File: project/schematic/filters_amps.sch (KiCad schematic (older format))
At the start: 19 parts

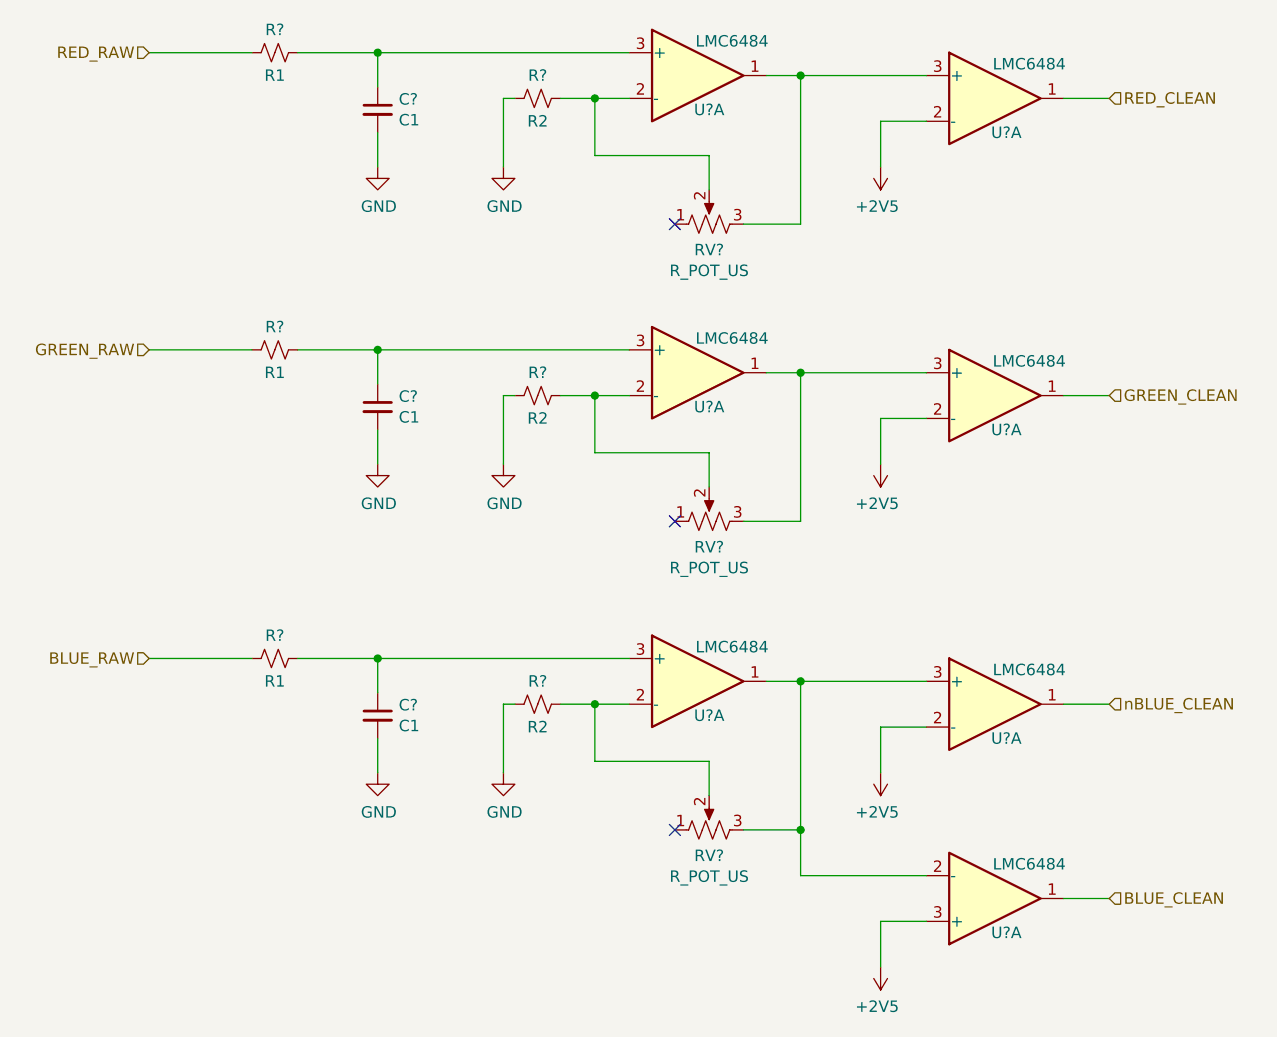
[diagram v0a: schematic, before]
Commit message: switch to high pass filters
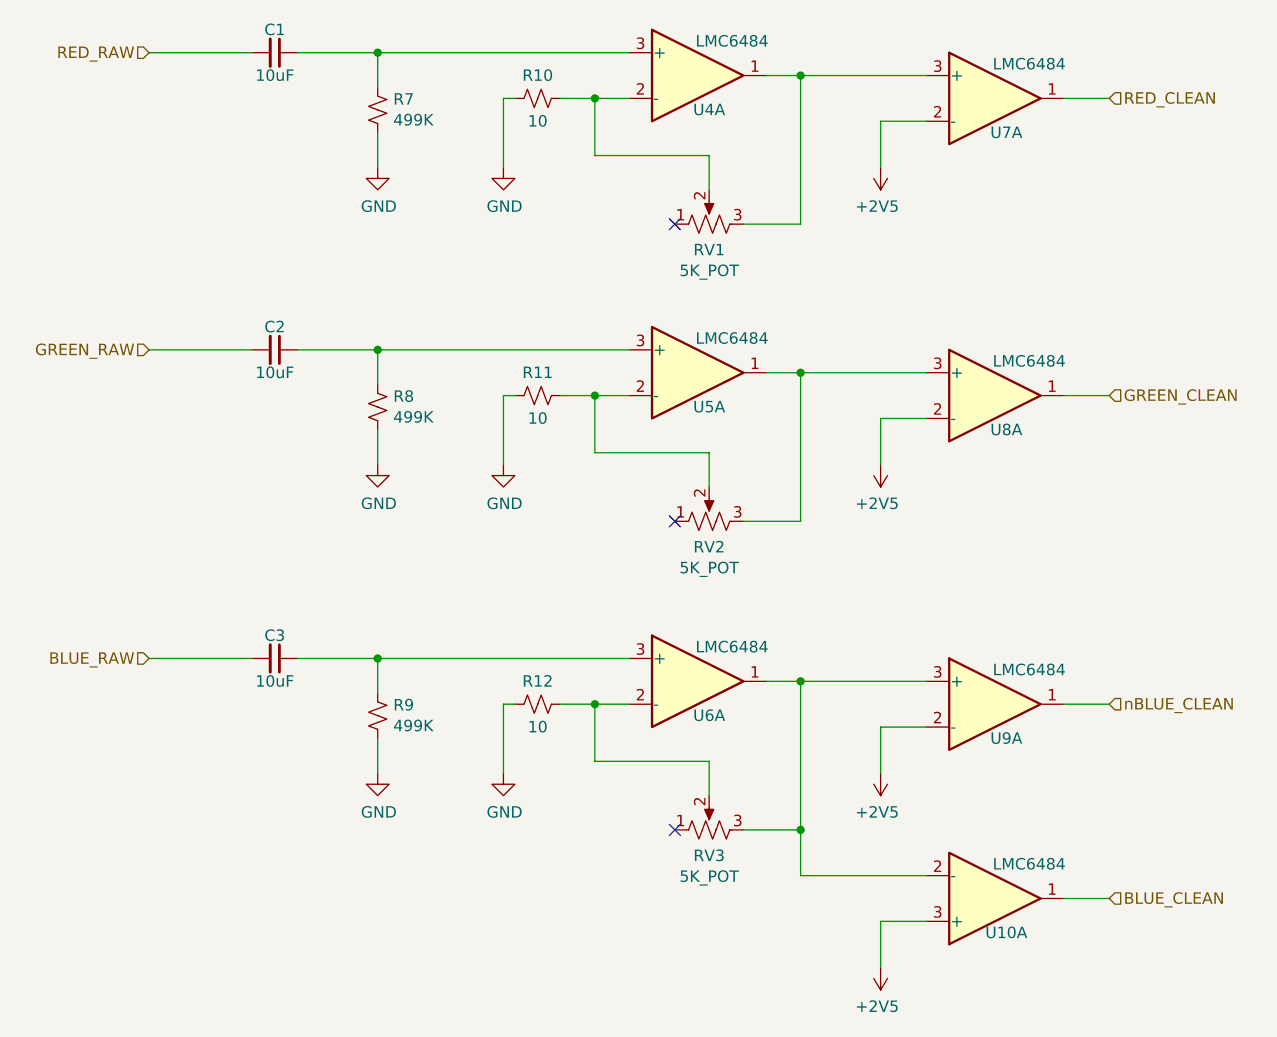
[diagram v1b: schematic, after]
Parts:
- removed C? (x3): C1, symbol Device:C_Small
- removed R? (x3): R1, symbol Device:R_Small_US
- added C1, C2, C3: 10uF, symbol Device:C_Small
- added R7, R8, R9: 499K, symbol Device:R_Small_US
- R10, R11, R12: renamed from R?; value R2 -> 10
- RV1, RV2, RV3: renamed from RV?; value R_POT_US -> 5K_POT
- gave numbers to parts that had none: 7
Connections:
- net BLUE_RAW: now also C3.2
- net GND: now also R7.2, R8.2, R9.2
- net GREEN_RAW: now also C2.2
- net RED_RAW: now also C1.2
- net at U6.3 (+): now also C3.1, R9.1
- net at U5.3 (+): now also C2.1, R8.1
- net at U4.3 (+): now also C1.1, R7.1
